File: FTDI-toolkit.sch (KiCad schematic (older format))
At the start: 88 parts, among them IC1 TLV70033DCKT, IC10 SN74LV1T125DCKR, IC11 SN74LV1T125DCKR, IC12 SN74LV1T125DCKR, IC13 74HC00BQ, IC15 TS5A3359, IC2 TLV70018DCKT, IC3 TS5A3359, IC4 SN74LV1T125DCKR, IC5 SN74LV1T125DCKR, IC6 SN74LV1T125DCKR, IC7 SN74LV1T125DCKR, IC9 SN74LV1T125DCKR, U1 FT2232H-56Q, Y1 MQ-6.000-12-30/30/

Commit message: Add new voltage translators, update layout
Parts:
- removed C13, C15, C7, C9: C_100n_0402_16V, antmicro-footprints:0402-cap, symbol antmicroCapacitors0402:C_100n_0402_16V
- removed IC10, IC11, IC12, IC4, IC5, IC6, IC7, IC9: SN74LV1T125DCKR, antmicro-footprints:SC70-5, symbol antmicroLogicTranslatorsLevelShifters:SN74LV1T125
- added U2, U3: TXB0104RUT, antmicro-footprints:Texas_R_PUQFN-N12, symbol antmicroLogicTranslatorsLevelShifters:TXB0104RUT
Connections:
- net labels added: ADBUS_OE, BDBUS_OE
- wire segments 309 -> 269
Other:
- note removed: "check OE conection"
- moved on the sheet: C10, C11, C12, C14, C16, C19, C20, C23, C24, C25, C26, C27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

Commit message: Add a prototype switch
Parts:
- added R10: R_510_0402, antmicro-footprints:0402-res, symbol antmicroResistors0402:R_510_0402
- added S1: JS202011SCQN, antmicro-footprints:Switch_Slide_JS202011SCQN, symbol antmicroSlideSwitches:JS202011SCQN
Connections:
- wire segments 269 -> 276
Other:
- note added: "OE design???\n\n"
- note added: "SWCLK\n"
- note added: "SWDAT"
- moved on the sheet: C10, C14, C16, C8, R11, R12, R14, R15, R19, RX_A1, RX_B1, TX_A1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

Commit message: Add SWD/JTAG switch, compress the board, DRC-clean
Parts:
- removed R19: R_10k_0402, antmicro-footprints:0402-res, symbol antmicroResistors0402:R_10k_0402
- removed R20: R_0R_0402, antmicro-footprints:0402-res, symbol antmicroResistors0402:R_0R_0402
- removed S1: JS202011SCQN, antmicro-footprints:Switch_Slide_JS202011SCQN, symbol antmicroSlideSwitches:JS202011SCQN
- added Q1: BC817, antmicro-footprints:SOT-23-3, symbol antmicroTransistorsBipolarSingle:BC817
- added R13: R_10k_0402, antmicro-footprints:0402-res, symbol antmicroResistors0402:R_10k_0402
- added R19: R_510_0402, antmicro-footprints:0402-res, symbol antmicroResistors0402:R_510_0402
- added SW1: JS202011JCQN, antmicro-footprints:JS202011JCQN, symbol antmicroSlideSwitches:JS202011JCQN
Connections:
- net labels removed: BDBUS_OE, UART_1_OE
- wire segments 276 -> 280
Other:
- note removed: "OE design???\n\n"
- moved on the sheet: R10, R11, R12, R14, R15, RX_A1, RX_B1, TX_A1, TX_B1

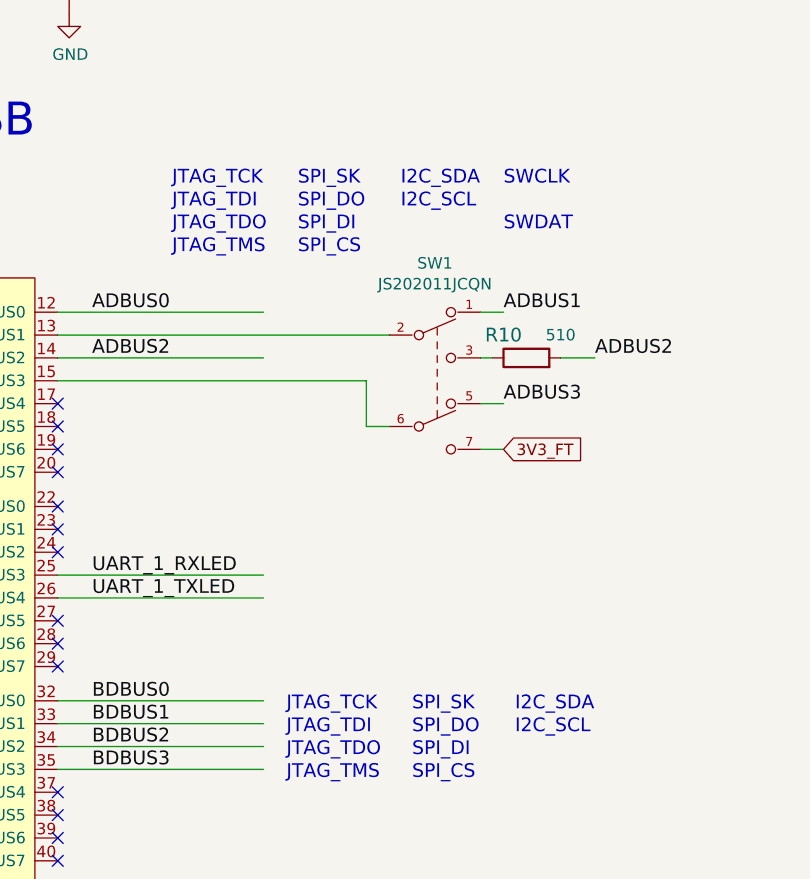
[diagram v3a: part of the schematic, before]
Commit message: Update interface description
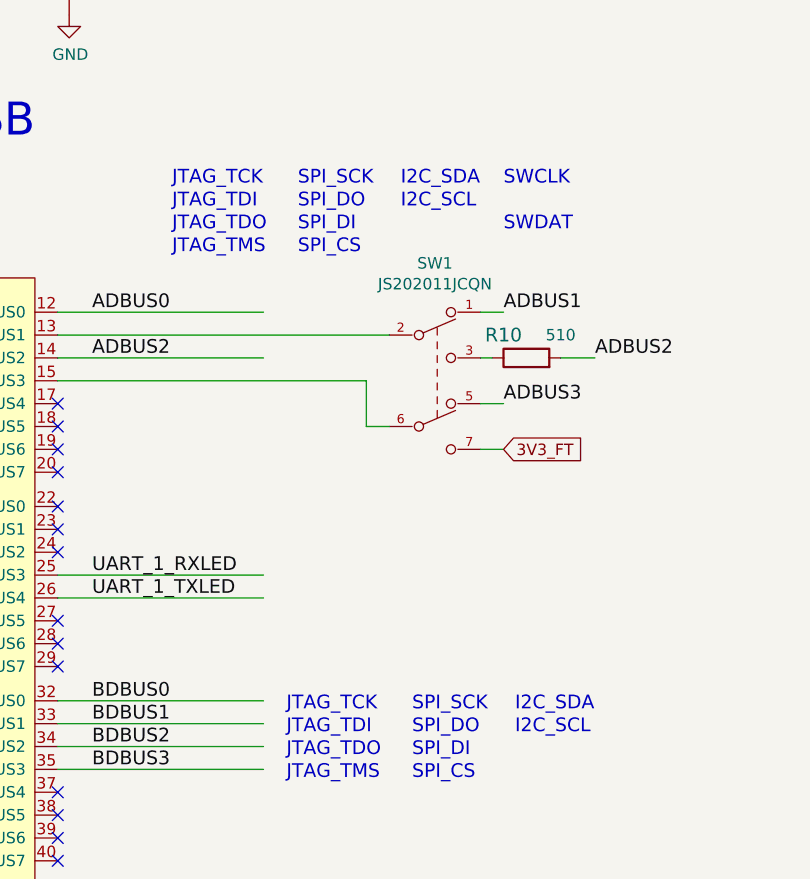
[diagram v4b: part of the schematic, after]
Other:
- note added: "SPI_SCK\n"
- note removed: "SPI_SK\n"
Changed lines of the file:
@@
 	5250 8800 6150 8800
 Text Notes 6300 6250 0    60   ~ 0
-SPI_SK\n
+SPI_SCK\n
 Text Notes 6300 6450 0    60   ~ 0
 SPI_DI\n
@@
 JTAG_TMS
 Text Notes 6800 8550 0    60   ~ 0
-SPI_SK\n
+SPI_SCK\n
 Text Notes 6800 8750 0    60   ~ 0
 SPI_DI\n

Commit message: Add ACBUS testpads, add ADBUS4-7 pinheader with VLT, swap oscillator
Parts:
- removed C17, C18: C_27p_0402, antmicro-footprints:0402-cap, symbol antmicroCapacitors0402:C_27p_0402
- removed Y1: MQ-6.000-12-30/30/, FTDI-toolkit:Crystal_5x7mm, symbol antmicroCrystals:CRYSTAL_6Mhz
- added C13, C7, C9: C_100n_0402_16V, antmicro-footprints:0402-cap, symbol antmicroCapacitors0402:C_100n_0402_16V
- added J4: 61300411121, antmicro-footprints:PinHeader_1x4_P2.54mm_Drill1.02mm, symbol antmicroRectangularConnectorsHeadersMalePins:61300411121
- added TP1, TP2, TP3, TP4, TP5, TP6, TP7, TP8: TP_SMD1MM, antmicro-footprints:Testpoint_smd_1mm, symbol antmicroTestPoints:TP_SMD1MM
- added U4: TXB0104RUT, Package_DFN_QFN:Texas_R_PUQFN-N12, symbol antmicroLogicTranslatorsLevelShifters:TXB0104RUT
- added Y1: ASFLMB-12.000MHZ-LC-T, antmicro-footprints:ASFLMB, symbol antmicroOscillators:ASFLMB-12.000MHZ-LC-T
- 1V8_A1, 1V8_B1, 3V3_A1, 3V3_B1, 5V0_A1, 5V0_B1, RX_A1, RX_B1, TX_A1, TX_B1, USB1: value KPT-1608SGC -> LG_L29K-G2J1-24-Z
- C1, C2, C5, C6: value 1u -> C_1u_0603
- D1: value TPD2E009DRTR -> TPD2E009
- D2: value ~ -> TPD6E05U06
- IC1: value TLV70033DCKT -> TLV700
- IC2: value TLV70018DCKT -> TLV700
- J1: value ~ -> WE_629105150521
- J2: value ~ -> 2X05
- J3: value ~ -> 2X08
- R9: value R_12k_0402_1% -> R_12k_0402
- SW1_A1: value ~ -> 1X03
- SW1_B1: value ~ -> 1X03; footprint FTDI-toolkit:MH_1X03_2.54 -> antmicro-footprints:MH_1X03_2.54
- U2, U3: footprint antmicro-footprints:Texas_R_PUQFN-N12 -> Package_DFN_QFN:Texas_R_PUQFN-N12
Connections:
- net labels added: ADBUS4, ADBUS5, ADBUS6, ADBUS7
- wire segments 280 -> 313
- no-connect marks 29 -> 20
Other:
- note added: "SPI_SI\n"
- note added: "SPI_SO\n"
- note added: "SPI_SS\n"
- note removed: "SPI_CS\n"
- note removed: "SPI_DI\n"
- note removed: "SPI_DO"
- moved on the sheet: C10, C14, C16, C8, Q1, R11, R12, R13, R14, R15, R19, RX_A1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

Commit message: Bump the revision
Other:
- note removed: "Review connections!!!!"
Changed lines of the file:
@@
 encoding utf-8
 Sheet 1 1
-Title "FTDI-Toolkit-SchDoc"
+Title "FTDI Toolkit"
 Date "04 03 2020"
-Rev ""
+Rev "1.1.0"
 Comp ""
-Comment1 ""
-Comment2 ""
+Comment1 "www.antmicro.com"
+Comment2 "Antmicro Ltd."
 Comment3 ""
 Comment4 ""
@@
 Text GLabel 2550 8950 0    50   Input ~ 0
 5V_USB
-Text Notes 13750 1750 0    118  ~ 24
-Review connections!!!!
 Wire Wire Line
 	1500 1900 1650 1900

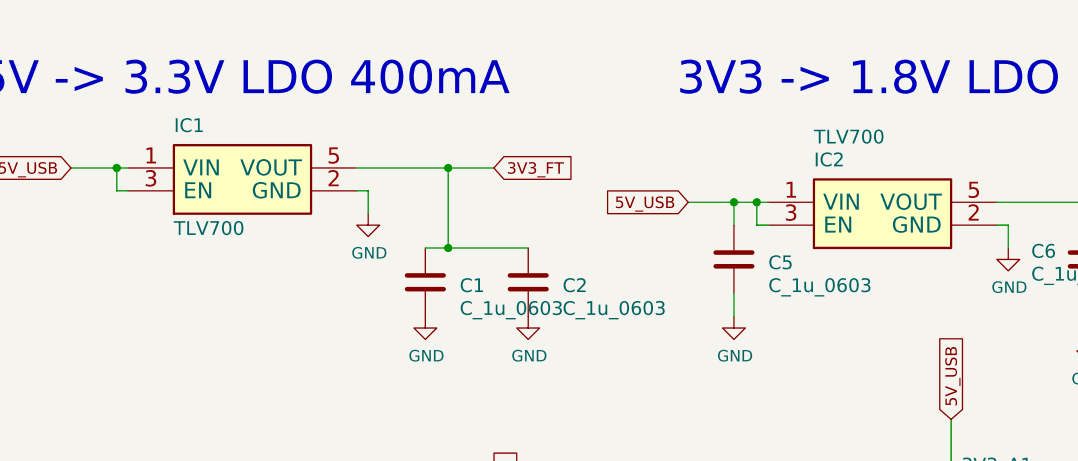
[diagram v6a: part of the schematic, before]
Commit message: Fix the libraries go get a complete BOM
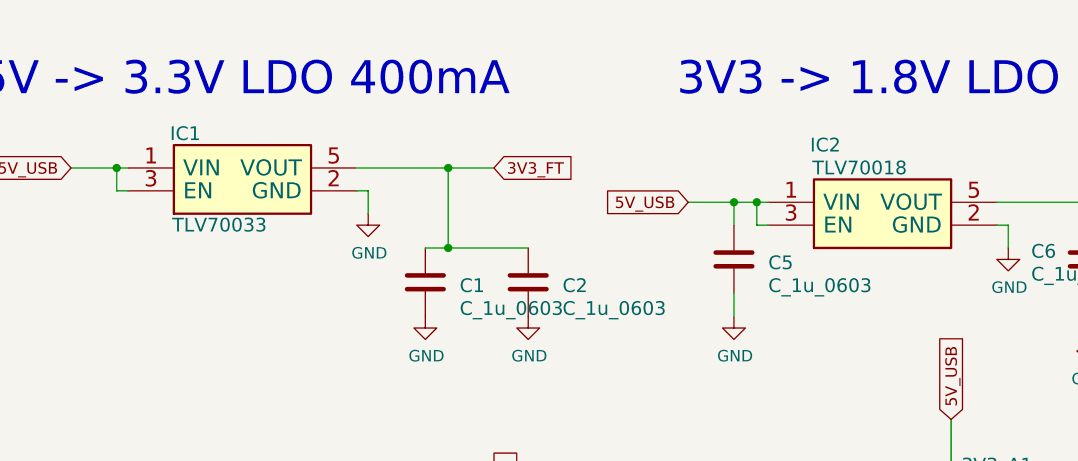
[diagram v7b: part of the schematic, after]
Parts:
- removed IC1, IC2: TLV700, antmicro-footprints:SC-70-5, symbol antmicroPMICVoltageRegulatorsLinear:TLV700
- added IC1: TLV70033, antmicro-footprints:SC-70-5, symbol antmicroPMICVoltageRegulatorsLinear:TLV70033
- added IC2: TLV70018, antmicro-footprints:SC-70-5, symbol antmicroPMICVoltageRegulatorsLinear:TLV70018
- D1: MPN (none) -> TPD2E009DRTR; Manufacturer (none) -> Texas Instruments
- IC13: MPN (none) -> 74HC00BQ; Manufacturer (none) -> Nexperia
- IC15, IC3: MPN (none) -> TS5A3359DCUR; Manufacturer (none) -> Texas Instruments
- J2: MPN (none) -> 61301021121; Manufacturer (none) -> Wurth Elektronik
- J3: MPN (none) -> 61301621121; Manufacturer (none) -> Wurth Elektronik
- Q1: MPN (none) -> BC817W,115; Manufacturer (none) -> Nexperia
- SW1: MPN (none) -> JS202011JCQN; Manufacturer (none) -> C&K
- SW1_A1, SW1_B1: MPN (none) -> 61300311121; Manufacturer (none) -> Wurth Elektronik
- U2, U3, U4: MPN (none) -> TXB0104RUTR; Manufacturer (none) -> Texas Instruments
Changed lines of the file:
@@
 F 2 "antmicro-footprints:DHVQFN14" H 8170 4600 60  0001 C CNN
 F 3 "" H 8170 4600 60  0000 C CNN
+F 4 "74HC00BQ" H 0   0   50  0001 C CNN "MPN"
+F 5 "Nexperia" H 0   0   50  0001 C CNN "Manufacturer"
 	1    7550 4100
 	1    0    0    -1
@@
 F 2 "antmicro-footprints:MH_2X08_2.54_RA" H 13650 4050 50  0001 C CNN
 F 3 "" H 13650 4050 50  0001 C CNN
+F 4 "61301621121" H 13650 4050 50  0001 C CNN "MPN"
+F 5 "Wurth Elektronik" H 0   0   50  0001 C CNN "Manufacturer"
 	1    13650 4050
 	1    0    0    -1
@@
 F 2 "antmicro-footprints:SOT-3" H 3400 1950 60  0001 C CNN
 F 3 "" H 3400 1950 60  0000 C CNN
+F 4 "TPD2E009DRTR" H 0   0   50  0001 C CNN "MPN"
+F 5 "Texas Instruments" H 0   0   50  0001 C CNN "Manufacturer"
 	1    2800 2250
 	0    1    1    0
@@
 F 2 "antmicro-footprints:SHF-105-01-X-D-SM" H 12400 2050 50  0001 C CNN
 F 3 "" H 12400 2050 50  0001 C CNN
+F 4 "61301021121" H 0   0   50  0001 C CNN "MPN"
+F 5 "Wurth Elektronik" H 0   0   50  0001 C CNN "Manufacturer"
 	1    12400 2050
 	1    0    0    -1
@@
 F 2 "antmicro-footprints:TS5A3359" H 3300 3950 60  0001 C CNN
 F 3 "" H 3300 3950 60  0000 C CNN
+F 4 "TS5A3359DCUR" H 0   0   50  0001 C CNN "MPN"
+F 5 "Texas Instruments" H 0   0   50  0001 C CNN "Manufacturer"
 	1    3300 4750
 	1    0    0    -1
@@
 F 2 "antmicro-footprints:TS5A3359" H 3300 2850 60  0001 C CNN
 F 3 "" H 3300 2850 60  0000 C CNN
+F 4 "TS5A3359DCUR" H 0   0   50  0001 C CNN "MPN"
+F 5 "Texas Instruments" H 0   0   50  0001 C CNN "Manufacturer"
 	1    3300 3650
 	1    0    0    -1
@@
 F 2 "antmicro-footprints:MH_1X03_2.54" H 1550 5000 50  0001 C CNN
 F 3 "" H 1550 5000 50  0001 C CNN
+F 4 "61300311121" H 0   0   50  0001 C CNN "MPN"
+F 5 "Wurth Elektronik" H 0   0   50  0001 C CNN "Manufacturer"
 	1    1550 5000
 	1    0    0    -1
@@
 F 2 "antmicro-footprints:MH_1X03_2.54" H 1550 4500 50  0001 C CNN
 F 3 "" H 1550 4500 50  0001 C CNN
+F 4 "61300311121" H 0   0   50  0001 C CNN "MPN"
+F 5 "Wurth Elektronik" H 0   0   50  0001 C CNN "Manufacturer"
 	1    1550 4500
 	1    0    0    -1
@@
 $EndComp
 $Comp
-L antmicroPMICVoltageRegulatorsLinear:TLV700 IC2
-U 1 1 5E5F7C4B
-P 9200 1950
-F 0 "IC2" H 8900 2200 60  0000 L BNN
-F 1 "TLV700" H 8900 2300 60  0000 L BNN
-F 2 "antmicro-footprints:SC-70-5" H 8900 2250 60  0001 C CNN
-F 3 "" H 8900 2250 60  0000 C CNN
-	1    9200 1950
-	1    0    0    -1
-$EndComp
-$Comp
-L antmicroPMICVoltageRegulatorsLinear:TLV700 IC1
-U 1 1 5E5F7C27
-P 6400 1800
-F 0 "IC1" H 6100 2050 60  0000 L BNN
-F 1 "TLV700" H 6100 1600 60  0000 L BNN
-F 2 "antmicro-footprints:SC-70-5" H 6100 1600 60  0001 C CNN
-F 3 "" H 6100 1600 60  0000 C CNN
-	1    6400 1800
-	1    0    0    -1
-$EndComp
-$Comp
 L antmicroInterfaceControllers:FT2232H-56Q U1
 U 1 1 5F74C0C3
@@
 F 2 "Package_DFN_QFN:Texas_R_PUQFN-N12" H 9500 6600 50  0001 C CNN
 F 3 "http://www.ti.com/lit/ds/symlink/txb0104.pdf" H 9610 7445 50  0001 C CNN
+F 4 "TXB0104RUTR" H 0   0   50  0001 C CNN "MPN"
+F 5 "Texas Instruments" H 0   0   50  0001 C CNN "Manufacturer"
 	1    9500 7350
 	1    0    0    -1
@@
 F 2 "Package_DFN_QFN:Texas_R_PUQFN-N12" H 9500 8750 50  0001 C CNN
 F 3 "http://www.ti.com/lit/ds/symlink/txb0104.pdf" H 9610 9595 50  0001 C CNN
+F 4 "TXB0104RUTR" H 0   0   50  0001 C CNN "MPN"
+F 5 "Texas Instruments" H 0   0   50  0001 C CNN "Manufacturer"
 	1    9500 9500
 	1    0    0    -1
@@
 F 26 "DPDT" H 6600 9800 50  0001 L CNN "throw configuration"
 F 27 "6V" H 6600 9900 50  0001 L CNN "voltage rating DC"
+F 28 "JS202011JCQN" H 0   0   50  0001 C CNN "MPN"
+F 29 "C&K" H 0   0   50  0001 C CNN "Manufacturer"
 	1    6600 6900
 	1    0    0    -1
@@
 F 2 "antmicro-footprints:SOT-23-3" H 15400 9225 50  0001 L CIN
 F 3 "" H 15200 9300 50  0001 L CNN
+F 4 "BC817W,115" H 0   0   50  0001 C CNN "MPN"
+F 5 "Nexperia" H 0   0   50  0001 C CNN "Manufacturer"
 	1    15200 9300
 	1    0    0    -1
@@
 F 2 "Package_DFN_QFN:Texas_R_PUQFN-N12" H 12250 6650 50  0001 C CNN
 F 3 "http://www.ti.com/lit/ds/symlink/txb0104.pdf" H 12360 7495 50  0001 C CNN
+F 4 "TXB0104RUTR" H 0   0   50  0001 C CNN "MPN"
+F 5 "Texas Instruments" H 0   0   50  0001 C CNN "Manufacturer"
 	1    12250 7400
 	1    0    0    -1
@@
 	0    -1   1    0
 $EndComp
+$Comp
+L antmicroPMICVoltageRegulatorsLinear:TLV70033 IC1
+U 1 1 5F45287D
+P 6400 1800
+F 0 "IC1" H 6150 2050 60  0000 C CNN
+F 1 "TLV70033" H 6300 1650 60  0000 C CNN
+F 2 "antmicro-footprints:SC-70-5" H 6800 1550 60  0001 C CNN
+F 3 "https://www.ti.com/lit/ds/symlink/tlv700.pdf?HQS=TI-null-null-mousermode-df-pf-null-wwe&ts=1597910921555&ref_url=https%253A%252F%252Fpl.mouser.com%252F" H 6400 1800 60  0001 C CNN
+F 4 "TLV70033DCKR" H 6400 1450 50  0001 C CNN "MPN"
+F 5 "Texas Instruments" H 0   0   50  0001 C CNN "Manufacturer"
+	1    6400 1800
+	1    0    0    -1
+$EndComp
+$Comp
+L antmicroPMICVoltageRegulatorsLinear:TLV70018 IC2
+U 1 1 5F453AE2
+P 9200 1950
+F 0 "IC2" H 8950 2300 60  0000 C CNN
+F 1 "TLV70018" H 9100 2200 60  0000 C CNN
+F 2 "antmicro-footprints:SC-70-5" H 9600 1700 60  0001 C CNN
+F 3 "https://www.ti.com/general/docs/suppproductinfo.tsp?distId=26&gotoUrl=http%3A%2F%2Fwww.ti.com%2Flit%2Fgpn%2Ftlv700" H 9200 1950 60  0001 C CNN
+F 4 "TLV70018DCKR" H 9200 1600 50  0001 C CNN "MPN"
+F 5 "Texas Instruments" H 0   0   50  0001 C CNN "Manufacturer"
+	1    9200 1950
+	1    0    0    -1
+$EndComp
 $EndSCHEMATC

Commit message: Fix MPN for JTAG
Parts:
- IC13: MPN 74HC00BQ -> 74HC00BQ,115
- J2: MPN 61301021121 -> SHF-105-01-L-D-SM; Manufacturer Wurth Elektronik -> Samtec
- Q1: MPN BC817W,115 -> BC817-16LT3G; Manufacturer Nexperia -> ON Semiconductor
- U1: MPN FT2232HQ -> FT2232HQ-TRAY
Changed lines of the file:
@@
 F 1 "74HC00BQ" H 7750 4900 60  0000 L BNN
 F 2 "antmicro-footprints:DHVQFN14" H 8170 4600 60  0001 C CNN
-F 3 "" H 8170 4600 60  0000 C CNN
-F 4 "74HC00BQ" H 0   0   50  0001 C CNN "MPN"
+F 3 "https://pl.mouser.com/datasheet/2/916/74HC_HCT00-1318972.pdf" H 8170 4600 60  0001 C CNN
+F 4 "74HC00BQ,115" H 0   0   50  0001 C CNN "MPN"
 F 5 "Nexperia" H 0   0   50  0001 C CNN "Manufacturer"
 	1    7550 4100
@@
 F 1 "2X08" H 13650 4050 50  0001 C CNN
 F 2 "antmicro-footprints:MH_2X08_2.54_RA" H 13650 4050 50  0001 C CNN
-F 3 "" H 13650 4050 50  0001 C CNN
+F 3 "https://www.we-online.com/catalog/datasheet/61301621121.pdf" H 13650 4050 50  0001 C CNN
 F 4 "61301621121" H 13650 4050 50  0001 C CNN "MPN"
 F 5 "Wurth Elektronik" H 0   0   50  0001 C CNN "Manufacturer"
@@
 F 1 "TPD2E009" V 3400 1950 60  0000 L BNN
 F 2 "antmicro-footprints:SOT-3" H 3400 1950 60  0001 C CNN
-F 3 "" H 3400 1950 60  0000 C CNN
+F 3 "https://www.ti.com/lit/ds/symlink/tpd2e009.pdf?ts=1597910439511&ref_url=https%253A%252F%252Fwww.google.com%252F" H 3400 1950 60  0001 C CNN
 F 4 "TPD2E009DRTR" H 0   0   50  0001 C CNN "MPN"
 F 5 "Texas Instruments" H 0   0   50  0001 C CNN "Manufacturer"
@@
 F 1 "2X05" H 12400 2050 50  0001 C CNN
 F 2 "antmicro-footprints:SHF-105-01-X-D-SM" H 12400 2050 50  0001 C CNN
-F 3 "" H 12400 2050 50  0001 C CNN
-F 4 "61301021121" H 0   0   50  0001 C CNN "MPN"
-F 5 "Wurth Elektronik" H 0   0   50  0001 C CNN "Manufacturer"
+F 3 "https://eu.mouser.com/datasheet/2/527/shf-1370134.pdf" H 12400 2050 50  0001 C CNN
+F 4 "SHF-105-01-L-D-SM" H 0   0   50  0001 C CNN "MPN"
+F 5 "Samtec" H 0   0   50  0001 C CNN "Manufacturer"
 	1    12400 2050
 	1    0    0    -1
@@
 F 1 "TS5A3359" H 3300 3950 60  0000 L BNN
 F 2 "antmicro-footprints:TS5A3359" H 3300 3950 60  0001 C CNN
-F 3 "" H 3300 3950 60  0000 C CNN
+F 3 "https://www.ti.com/general/docs/suppproductinfo.tsp?distId=26&gotoUrl=http%3A%2F%2Fwww.ti.com%2Flit%2Fgpn%2Fts5a3359" H 3300 3950 60  0001 C CNN
 F 4 "TS5A3359DCUR" H 0   0   50  0001 C CNN "MPN"
 F 5 "Texas Instruments" H 0   0   50  0001 C CNN "Manufacturer"
@@
 F 1 "TS5A3359" H 3300 2850 60  0000 L BNN
 F 2 "antmicro-footprints:TS5A3359" H 3300 2850 60  0001 C CNN
-F 3 "" H 3300 2850 60  0000 C CNN
+F 3 "https://www.ti.com/general/docs/suppproductinfo.tsp?distId=26&gotoUrl=http%3A%2F%2Fwww.ti.com%2Flit%2Fgpn%2Fts5a3359" H 3300 2850 60  0001 C CNN
 F 4 "TS5A3359DCUR" H 0   0   50  0001 C CNN "MPN"
 F 5 "Texas Instruments" H 0   0   50  0001 C CNN "Manufacturer"
@@
 F 1 "1X03" H 1550 5000 50  0001 C CNN
 F 2 "antmicro-footprints:MH_1X03_2.54" H 1550 5000 50  0001 C CNN
-F 3 "" H 1550 5000 50  0001 C CNN
+F 3 "https://www.we-online.com/catalog/datasheet/61300311121.pdf" H 1550 5000 50  0001 C CNN
 F 4 "61300311121" H 0   0   50  0001 C CNN "MPN"
 F 5 "Wurth Elektronik" H 0   0   50  0001 C CNN "Manufacturer"
@@
 F 1 "1X03" H 1550 4500 50  0001 C CNN
 F 2 "antmicro-footprints:MH_1X03_2.54" H 1550 4500 50  0001 C CNN
-F 3 "" H 1550 4500 50  0001 C CNN
+F 3 "https://www.we-online.com/catalog/datasheet/61300311121.pdf" H 1550 4500 50  0001 C CNN
 F 4 "61300311121" H 0   0   50  0001 C CNN "MPN"
 F 5 "Wurth Elektronik" H 0   0   50  0001 C CNN "Manufacturer"
@@
 F 3 "https://www.ftdichip.com/Support/Documents/DataSheets/ICs/DS_FT2232H.pdf" H 4650 9350 60  0001 L CNN
 F 4 "FTDI" H 4650 10100 60  0001 L CNN "Manufacturer"
-F 5 "FT2232HQ" H 4650 9500 60  0001 L CNN "MPN"
+F 5 "FT2232HQ-TRAY" H 4650 9500 60  0001 L CNN "MPN"
 	1    4450 8950
 	1    0    0    -1
@@
 F 1 "BC817" H 15391 9255 50  0000 L CNN
 F 2 "antmicro-footprints:SOT-23-3" H 15400 9225 50  0001 L CIN
-F 3 "" H 15200 9300 50  0001 L CNN
-F 4 "BC817W,115" H 0   0   50  0001 C CNN "MPN"
-F 5 "Nexperia" H 0   0   50  0001 C CNN "Manufacturer"
+F 3 "https://assets.nexperia.com/documents/data-sheet/BC817W_SER.pdf" H 15200 9300 50  0001 L CNN
+F 4 "BC817-16LT3G" H 0   0   50  0001 C CNN "MPN"
+F 5 "ON Semiconductor" H 0   0   50  0001 C CNN "Manufacturer"
 	1    15200 9300
 	1    0    0    -1
